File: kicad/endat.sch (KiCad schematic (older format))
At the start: 31 parts, among them J1001 tblock2x6, U1001 ADM2483, U1002 ADM2483, U1003 ADM2483, U1004 ADM2483

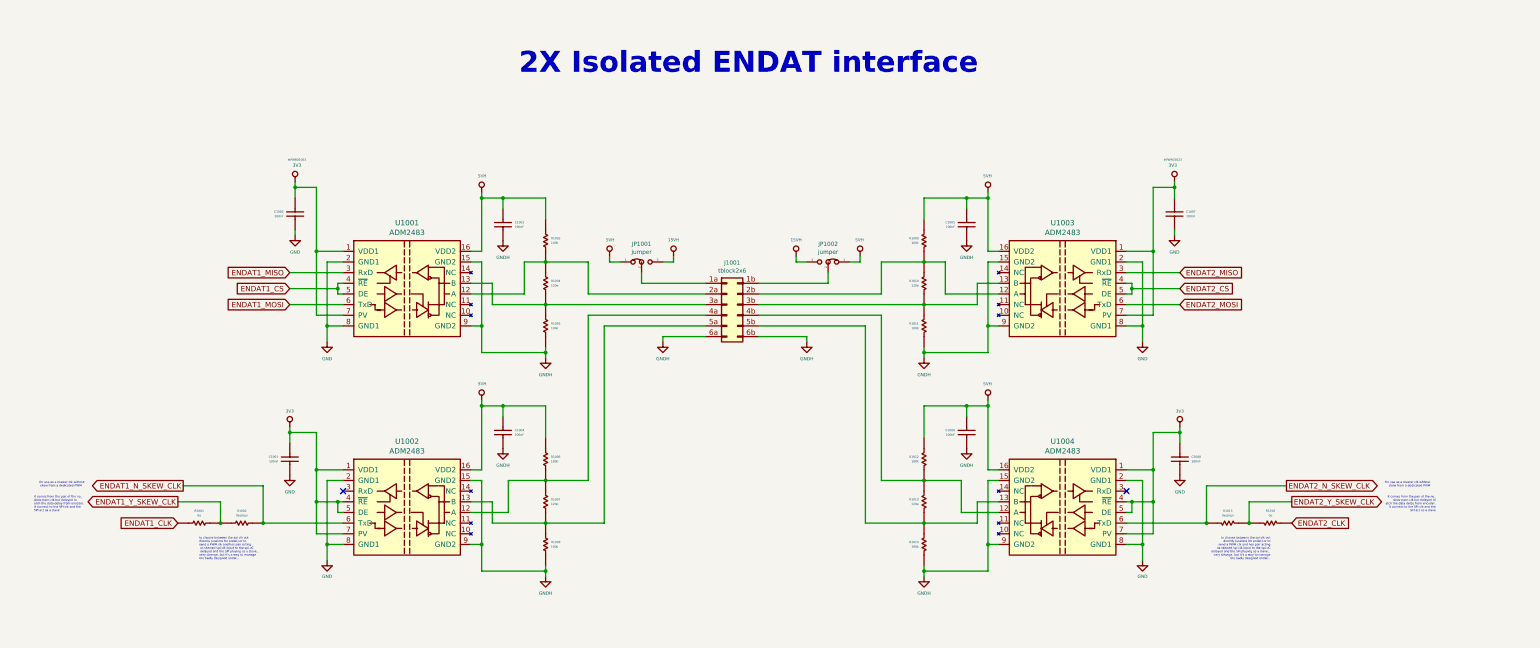
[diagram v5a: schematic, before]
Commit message: I forgot that QUEP was diferential!! all to back....
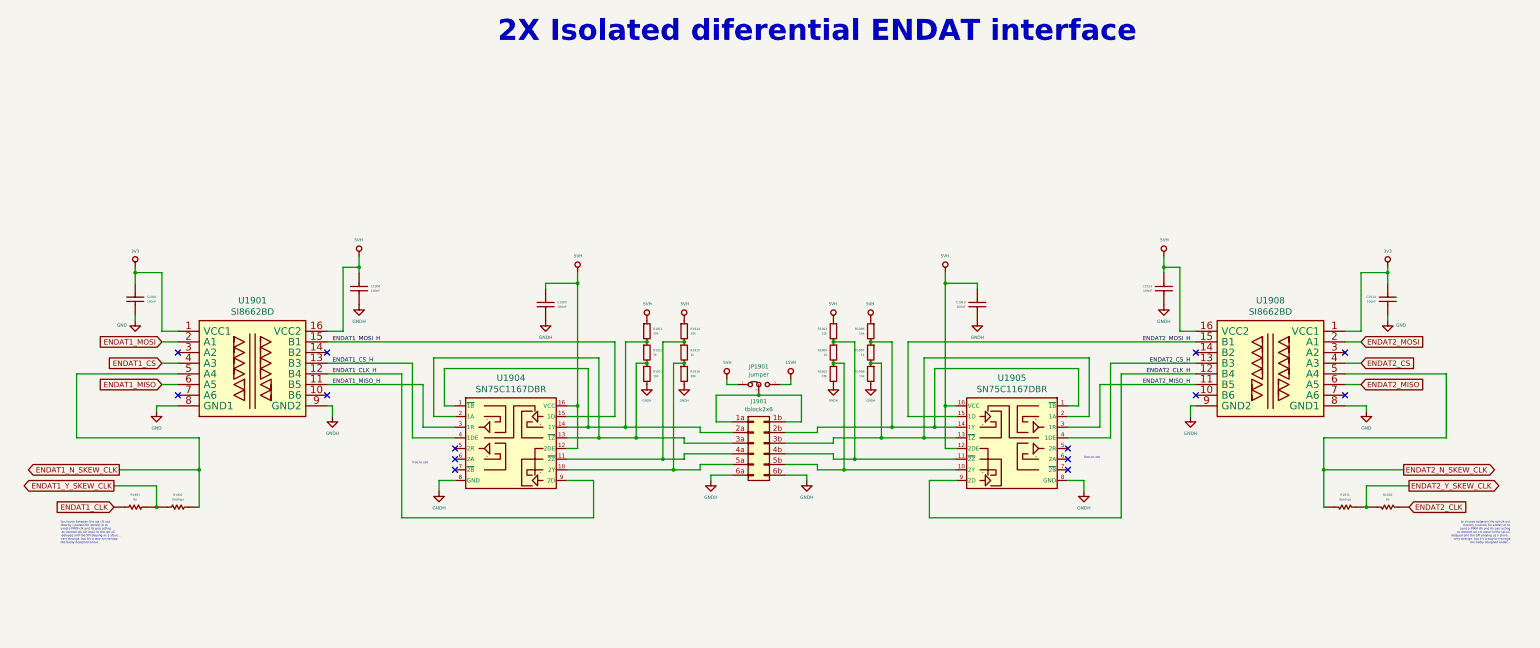
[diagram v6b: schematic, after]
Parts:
- removed C1001, C1002, C1003, C1004, C1005, C1006, C1007, C1008: 100nF, servo:C_0603_1608Metric, symbol servo:Capacitor
- removed J1001: tblock2x6, servo:tblock02x06, symbol servo:tblock2x6
- removed JP1001, JP1002: jumper, Jumper:SolderJumper-3_P1.3mm_Open_RoundedPad1.0x1.5mm, symbol servo:Jumper_3_Bridged12
- removed R1001, R1016: 0e, Resistor_SMD:R_0603_1608Metric, symbol servo:Resistor
- removed R1002, R1015: 0e(dnp), Resistor_SMD:R_0603_1608Metric, symbol servo:Resistor
- removed R1003, R1005, R1006, R1008, R1009, R1011, R1012, R1014: 100k, Resistor_SMD:R_0603_1608Metric, symbol servo:Resistor
- removed R1004, R1007, R1010, R1013: 120e, Resistor_SMD:R_0603_1608Metric, symbol servo:Resistor
- removed U1001, U1002, U1003, U1004: ADM2483, Package_SO:SOIC-16W_7.5x10.3mm_P1.27mm, symbol servo:ADM2483
- added C1901, C1904, C1905, C1910, C1913, C1914: 100nF, servo:C_0603_1608Metric, symbol servo:Capacitor
- added J1901: tblock2x6, Connector_Phoenix_MC:PhoenixContact_MC_1,5_6-G-3.81_1x06_P3.81mm_Horizontal, symbol servo:tblock2x6
- added JP1901: jumper, Jumper:SolderJumper-3_P1.3mm_Open_RoundedPad1.0x1.5mm, symbol servo:Jumper_3_Bridged12
- added R1901, R1932: 0e, Resistor_SMD:R_0603_1608Metric, symbol servo:Resistor
- added R1902, R1931: 0e(dnp), Resistor_SMD:R_0603_1608Metric, symbol servo:Resistor
- added R1903, R1905, R1906, R1908, R1911, R1913, R1914, R1916: 10k, Resistor_SMD:R_0603_1608Metric, symbol servo:R_Small
- added R1904, R1907, R1912, R1915: 1k, Resistor_SMD:R_0603_1608Metric, symbol servo:R_Small
- added U1901, U1908: SI8662BD, Package_SO:SOIC-16W_7.5x10.3mm_P1.27mm, symbol servo:SI8662BD
- added U1904, U1905: SN75C1167DBR, Package_SO:SSOP-16_5.3x6.2mm_P0.65mm, symbol servo:SN75C1167DBR
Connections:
- net 15VH: now also JP1901.3 (B)
- net 3V3: now also C1901.2 (Capacitor), C1914.2 (Capacitor), U1901.1 (VCC1), U1908.1 (VCC1)
- net 5VH: now also C1904.2 (Capacitor), C1905.2 (Capacitor), C1910.2 (Capacitor), C1913.2 (Capacitor), JP1901.1 (A), R1903.1, R1906.1, R1911.1, R1914.1, U1901.16 (VCC2), U1904.12 (2DE), U1904.16 (VCC), U1905.12 (2DE), U1905.16 (VCC), U1908.16 (VCC2)
- net ENDAT1_CLK: now also R1901.1
- net ENDAT1_CS: now also U1901.4 (A3)
- net ENDAT1_MISO: now also U1901.6 (A5)
- net ENDAT1_MOSI: now also U1901.2 (A1)
- net ENDAT1_N_SKEW_CLK: now also R1902.2, U1901.5 (A4)
- net ENDAT1_Y_SKEW_CLK: now also R1901.2, R1902.1
- net ENDAT2_CLK: now also R1932.1
- net ENDAT2_CS: now also U1908.4 (A3)
- net ENDAT2_MISO: now also U1908.6 (A5)
- net ENDAT2_MOSI: now also U1908.2 (A1)
- net ENDAT2_N_SKEW_CLK: now also R1931.2, U1908.5 (A4)
- net ENDAT2_Y_SKEW_CLK: now also R1931.1, R1932.2
- net GND: now also C1901.1, C1914.1, U1901.8 (GND1), U1908.8 (GND1)
- net GNDH: now also C1904.1, C1905.1, C1910.1, C1913.1, J1901.6a (Pin_6a), J1901.6b (Pin_6b), R1905.2, R1908.2, R1913.2, R1916.2, U1901.9 (GND2), U1904.8 (GND), U1905.8 (GND), U1908.9 (GND2)
- new net: J1901.2a (Pin_2a), R1911.2, R1912.1, U1904.1 (~1B), U1904.14 (1Y)
- new net: J1901.5a (Pin_5a), R1915.2, R1916.1, U1904.10 (2Y)
- new net: J1901.4a (Pin_4a), R1914.2, R1915.1, U1904.11 (~2Z)
- new net: J1901.3a (Pin_3a), R1912.2, R1913.1, U1904.13 (~1Z), U1904.2 (1A)
- new net: J1901.2b (Pin_2b), R1906.2, R1907.1, U1905.1 (~1B), U1905.14 (1Y)
- new net: J1901.3b (Pin_3b), R1907.2, R1908.1, U1905.13 (~1Z), U1905.2 (1A)
- new net: J1901.4b (Pin_4b), R1903.2, R1904.1, U1905.11 (~2Z)
- new net: J1901.5b (Pin_5b), R1904.2, R1905.1, U1905.10 (2Y)
- new net: J1901.1a (Pin_1a), J1901.1b (Pin_1b), JP1901.2 (C)
- new net ENDAT1_CLK_H: U1901.12 (B4), U1904.9 (2D)
- new net ENDAT1_CS_H: U1901.13 (B3), U1904.4 (1DE)
- new net ENDAT1_MISO_H: U1901.11 (B5), U1904.3 (1R)
- new net ENDAT1_MOSI_H: U1901.15 (B1), U1904.15 (1D)
- new net ENDAT2_CLK_H: U1905.9 (2D), U1908.12 (B4)
- new net ENDAT2_CS_H: U1905.4 (1DE), U1908.13 (B3)
- new net ENDAT2_MISO_H: U1905.3 (1R), U1908.11 (B5)
- new net ENDAT2_MOSI_H: U1905.15 (1D), U1908.15 (B1)
- no-connect marks 2 -> 14
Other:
- note added: "2X Isolated diferential ENDAT interface"
- note added: "free to use\n"
- note added: "to choose between the spi clk out \ndirectly (useless for endat) or to \nsend a PWM clk and its pair acting\n as skewed spi clk input to the spi uC\n delayed and the SPI playing as a slave...\nvery strange, but it's a way to manage \nthe badly designed endat...\n"
- note removed: "2X Isolated ENDAT interface"
- note removed: "for usa as a master clk without\n skew from a dedicated PWM\n\n"
- note removed: "it comes from the pair of the no_\nskew pwm clk but delayed to \natch the data delay from encoder.\nIt connect to the SPI clk and the \nSPI act as a slave"
- note removed: "to choose between the spi clk out \ndirectly (useless for endat) or to \nsend a PWM clk and hes pair acting\n as skewed spi clk input to the spi uC\n delayed and the SPI playing as a slave...\nvery strange, but it's a way to manage \nthe badly designed endat...\n"

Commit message: changed 200mils connector to 150mils 'cause space constraints
I've decided to change 200 mils input connector for encat, rs485 and so
for 150mis 'cose it doesn't deliver so much current and I'd save some
space in the board. I've added the step/dir differential interface that
I've fotgot, and also add differential input to all signals of
incremental encoder interface A/B/I/S .. now lets rock
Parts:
- J1901: footprint Connector_Phoenix_MC:PhoenixContact_MC_1,5_6-G-3.81_1x06_P3.81mm_Horizontal -> servo:tblock02x6_3.81
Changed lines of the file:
@@
 F 0 "J1901" H 8350 5493 39  0000 C CNN
 F 1 "tblock2x6" H 8350 5418 39  0000 C CNN
-F 2 "Connector_Phoenix_MC:PhoenixContact_MC_1,5_6-G-3.81_1x06_P3.81mm_Horizontal" H 8250 5300 50  0001 C CNN
+F 2 "servo:tblock02x6_3.81" H 8250 5300 50  0001 C CNN
 F 3 "../doc/datasheets/tblock2rows.pdf" H 8350 5400 50  0001 C CNN
 	1    8300 5100

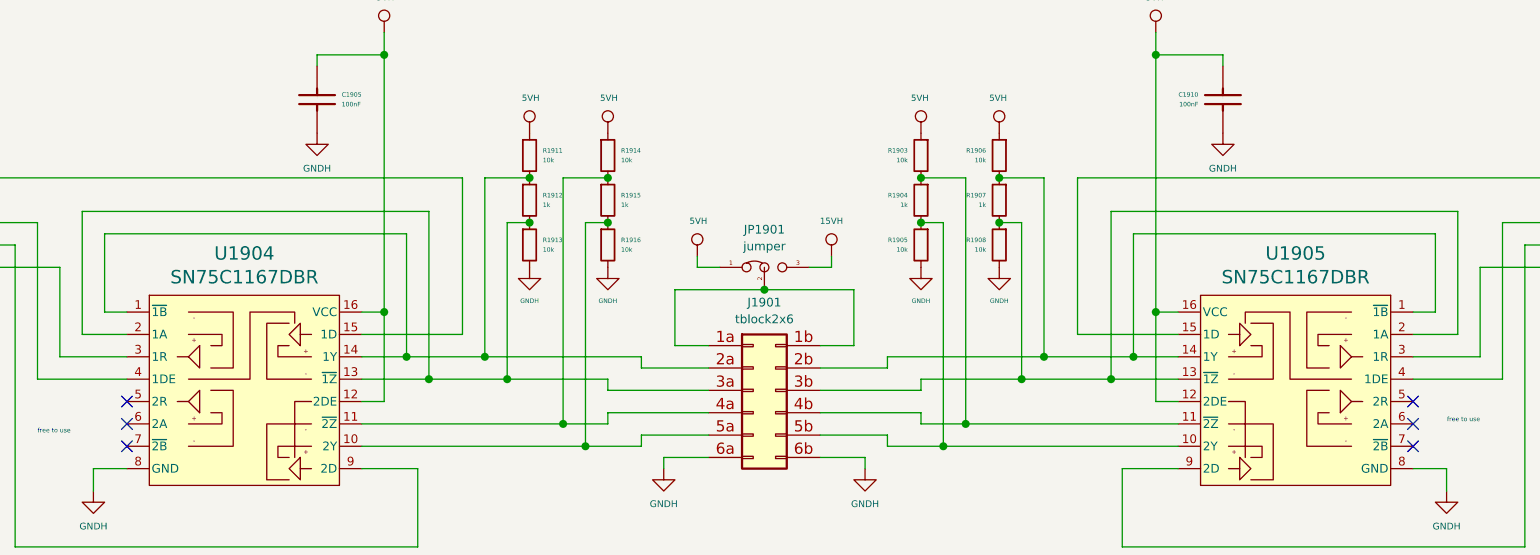
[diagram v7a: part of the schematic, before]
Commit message: placing smmall capacitors and resistors nerar his group
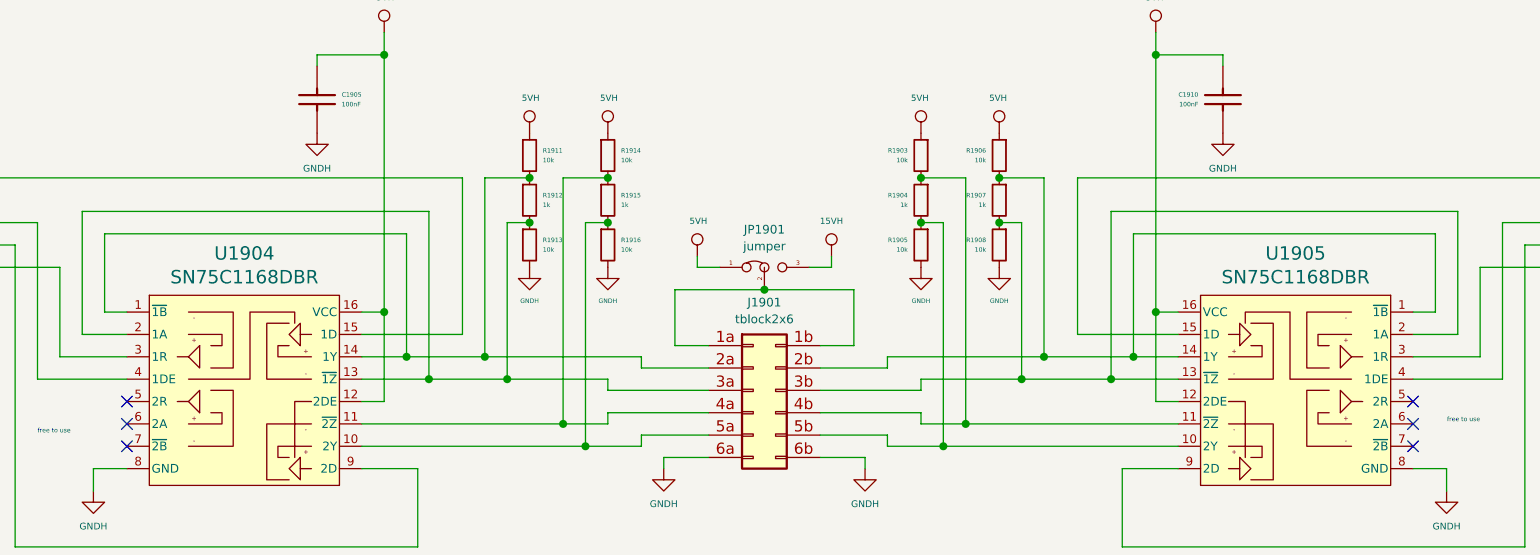
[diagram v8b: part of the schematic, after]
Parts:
- U1904, U1905: value SN75C1167DBR -> SN75C1168DBR; footprint Package_SO:SSOP-16_5.3x6.2mm_P0.65mm -> Package_SO:SOIC-16W_5.3x10.2mm_P1.27mm
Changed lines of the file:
@@
 AR Path="/5F8D42C2/5E26347A" Ref="U1904"  Part="1"
 F 0 "U1904" H 6025 5712 60  0000 C CNN
-F 1 "SN75C1167DBR" H 6025 5606 60  0000 C CNN
-F 2 "Package_SO:SSOP-16_5.3x6.2mm_P0.65mm" H 5900 5665 60  0001 C CNN
+F 1 "SN75C1168DBR" H 6025 5606 60  0000 C CNN
+F 2 "Package_SO:SOIC-16W_5.3x10.2mm_P1.27mm" H 5900 5665 60  0001 C CNN
 F 3 "../doc/datasheets/sn65c1168.pdf" H 5900 5825 60  0001 C CNN
 	1    6000 5100
@@
 AR Path="/5F8D42C2/5F749BC7" Ref="U1905"  Part="1"
 F 0 "U1905" H 10775 5712 60  0000 C CNN
-F 1 "SN75C1167DBR" H 10775 5606 60  0000 C CNN
-F 2 "Package_SO:SSOP-16_5.3x6.2mm_P0.65mm" H 10650 5665 60  0001 C CNN
-F 3 "" H 10650 5825 60  0001 C CNN
+F 1 "SN75C1168DBR" H 10775 5606 60  0000 C CNN
+F 2 "Package_SO:SOIC-16W_5.3x10.2mm_P1.27mm" H 10650 5665 60  0001 C CNN
+F 3 "../doc/datasheets/sn65c1168.pdf" H 10650 5825 60  0001 C CNN
 	1    10750 5100
 	-1   0    0    -1
